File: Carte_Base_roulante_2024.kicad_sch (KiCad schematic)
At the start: 18 parts, among them J1 Screw_Terminal_01x02, J2 Screw_Terminal_01x02, J3 Screw_Terminal_01x02, U1 STM32G484RETx, U4 R-78E5.0-1.0

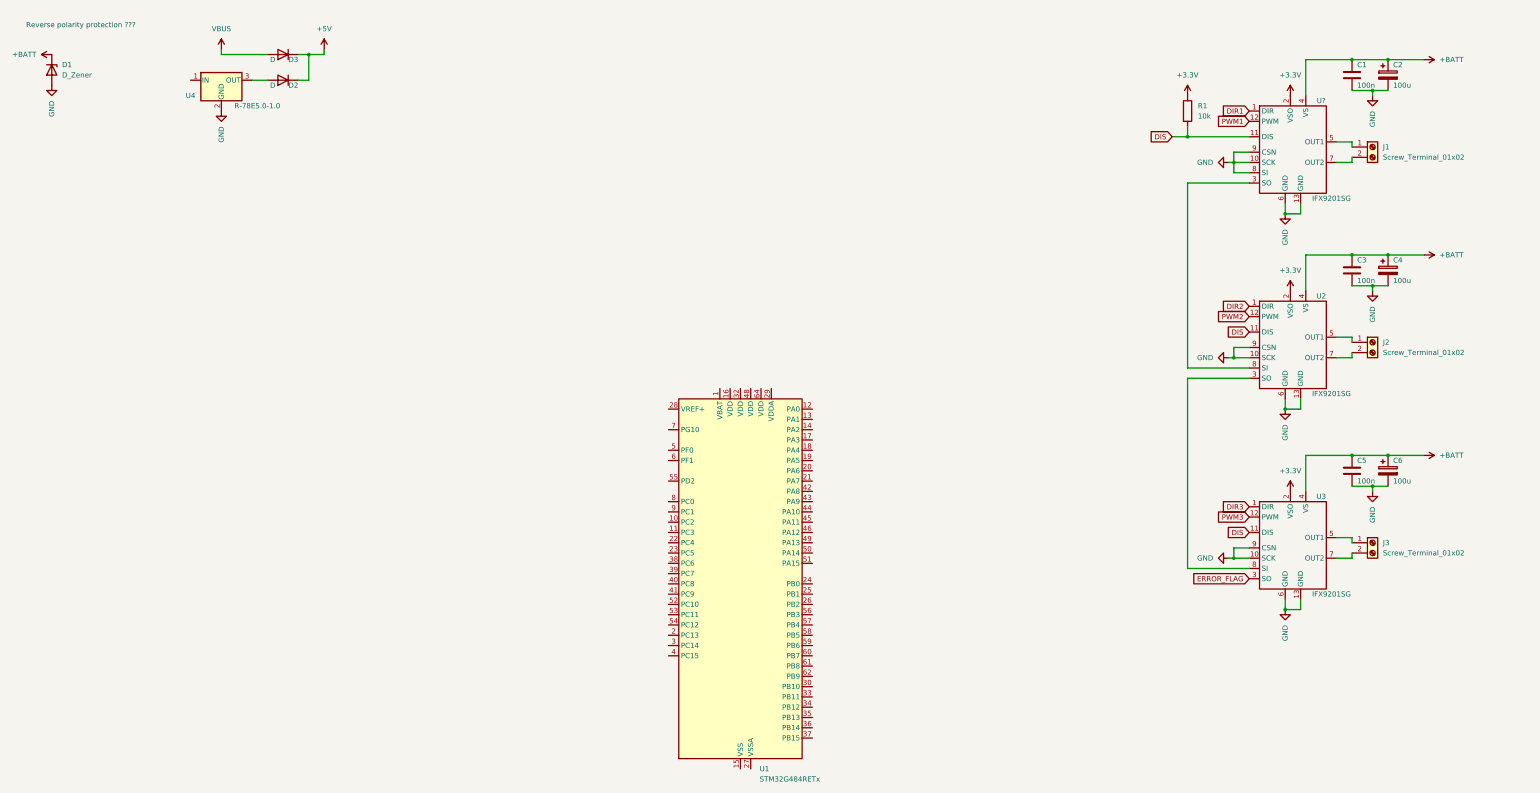
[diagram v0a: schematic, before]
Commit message: add capacitors
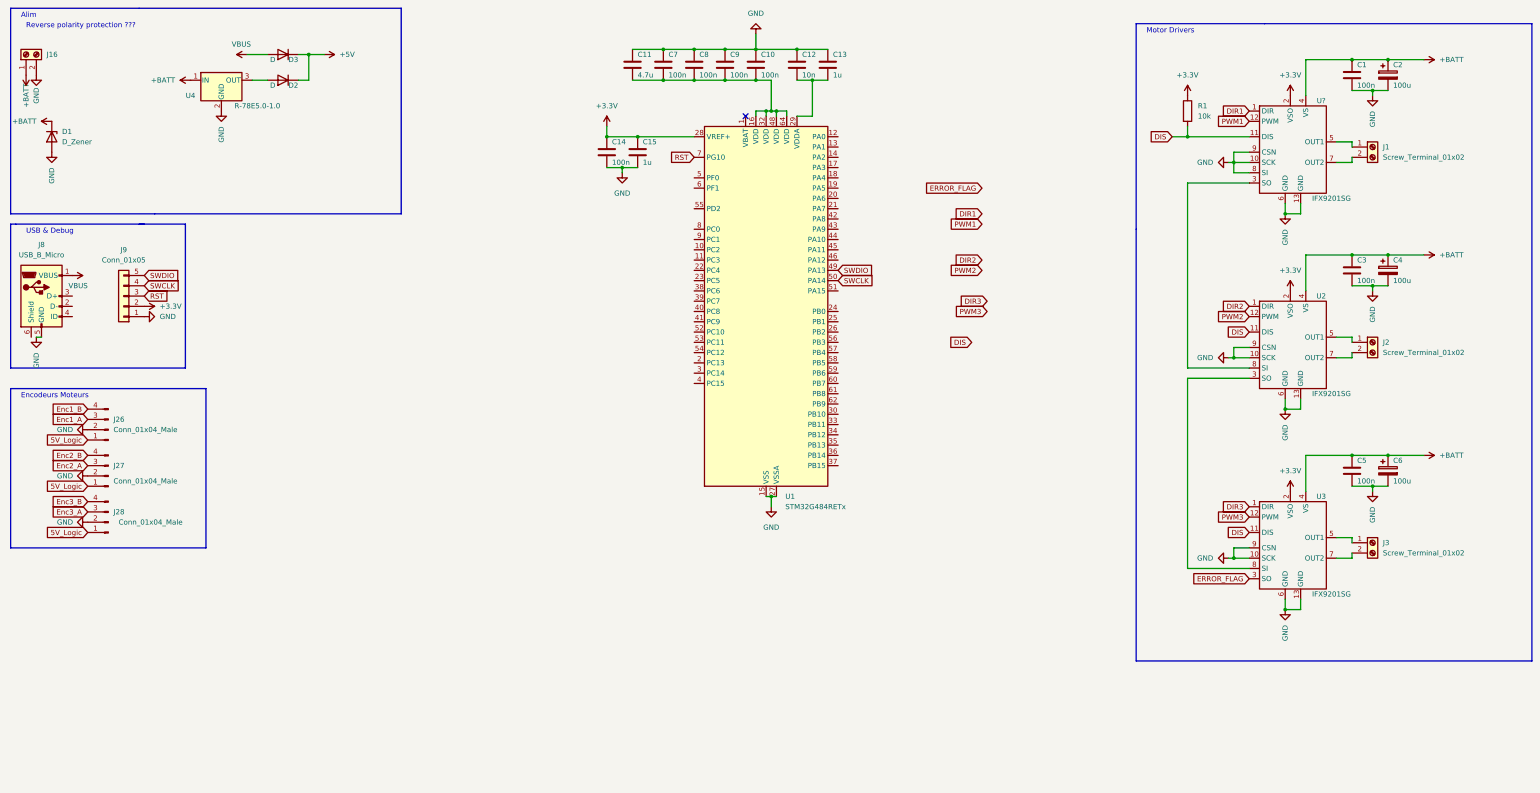
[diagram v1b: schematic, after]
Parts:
- added C10, C14, C7, C8, C9: 100n, Capacitor_SMD:C_0805_2012Metric, symbol Device:C
- added C11: 4.7u, symbol Device:C
- added C12: 10n, symbol Device:C
- added C13, C15: 1u, symbol Device:C
- added J16: Screw_Terminal_01x02, TerminalBlock:TerminalBlock_bornier-2_P5.08mm, symbol Connector:Screw_Terminal_01x02
- added J26, J27, J28: Conn_01x04_Male, library:HE14_EMBASE_1x04, symbol Connector:Conn_01x04_Male
- added J8: USB_B_Micro, symbol Connector:USB_B_Micro
- added J9: Conn_01x05, Connector_Molex:Molex_CLIK-Mate_502382-0570_1x05-1MP_P1.25mm_Vertical, symbol Connector_Generic:Conn_01x05
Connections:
- net +3.3V: now also U1.28 (VREF+), C14.1, C15.1, J9.2 (Pin_2)
- net +BATT: now also U4.1 (IN), J16.1 (Pin_1)
- net GND: now also U1.15 (VSS), U1.27 (VSSA), U1.31 (VSS), U1.47 (VSS), U1.63 (VSS), C10.1, C11.1, C12.1, C13.1, C14.2, C15.2, C7.1, C8.1, C9.1, J16.2 (Pin_2), J26.2 (Pin_2), J27.2 (Pin_2), J28.2 (Pin_2), J8.5 (GND), J9.1 (Pin_1)
- net VBUS: now also J8.1 (VBUS)
- net at U1.16 (VDD): now also U1.32 (VDD), U1.48 (VDD), U1.64 (VDD), C10.2, C11.2, C7.2, C8.2, C9.2
- net at U1.29 (VDDA): now also C12.2, C13.2
- net SWDIO: now reaches U1.49 (PA13)
- net SWDIO: now also J9.5 (Pin_5)
- net SWCLK: now reaches U1.50 (PA14)
- net SWCLK: now also J9.4 (Pin_4)
- net RST: now reaches U1.7 (PG10)
- net RST: now also J9.3 (Pin_3)
- new net 5V_Logic: J26.1 (Pin_1), J27.1 (Pin_1), J28.1 (Pin_1)
- new net Enc1_A: J26.3 (Pin_3)
- new net Enc1_B: J26.4 (Pin_4)
- new net Enc2_A: J27.3 (Pin_3)
- new net Enc2_B: J27.4 (Pin_4)
- new net Enc3_A: J28.3 (Pin_3)
- new net Enc3_B: J28.4 (Pin_4)
- no-connect marks 0 -> 1
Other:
- note added: "Alim"
- note added: "Encodeurs Moteurs"
- note added: "Motor Drivers"
- note added: "USB & Debug"
- moved on the sheet: D1, U1

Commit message: IMU + SPI
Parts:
- added U5: LSM6DSL, Package_LGA:LGA-14_3x2.5mm_P0.5mm_LayoutBorder3x4y, symbol Sensor_Motion:LSM6DSL
- U?: RS (none) -> https://fr.rs-online.com/web/p/drivers-de-moteur/1702333
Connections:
- net 5V_Logic is gone; now on net +5V: J26.1 (Pin_1), J27.1 (Pin_1), J28.1 (Pin_1)
- net DIR1: now also U1.41 (PC9)
- net DIR2: now also U1.44 (PA10)
- net DIR3: now also U1.46 (PA12)
- net DIS: now also U1.40 (PC8)
- net ERROR_FLAG: now also U1.39 (PC7)
- net Enc1_A: now also U1.12 (PA0)
- net Enc1_B: now also U1.13 (PA1)
- net Enc2_A: now also U1.20 (PA6)
- net Enc2_B: now also U1.21 (PA7)
- net Enc3_A: now also U1.60 (PB7)
- net Enc3_B: now also U1.59 (PB6)
- net PWM1: now also U1.42 (PA8)
- net PWM2: now also U1.43 (PA9)
- net PWM3: now also U1.45 (PA11)
- net UART4_TX: now reaches U1.52 (PC10)
- net UART4_RX: now reaches U1.53 (PC11)
- new net: U5.6 (GND), U5.7 (GND)
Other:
- note added: "Reverse polarity protection ??? Normalement on ne devrait pas brancher la batterie a l'enver donc non ?"
- note added: "Stm32"
- note removed: "Reverse polarity protection ???"
- moved on the sheet: C10, C11, C12, C13, C14, C15, C7, C8, C9, D2, D3, J16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

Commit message: usb + protection + cristal + leds + adc
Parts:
- removed J8: USB_B_Micro, symbol Connector:USB_B_Micro
- added C16, C17, C18: 100n, Capacitor_SMD:C_0805_2012Metric, symbol Device:C
- added D4: D_Zener, symbol Device:D_Zener
- added D5, D6, D7: LED, LED_SMD:LED_0603_1608Metric_Pad1.05x0.95mm_HandSolder, symbol Device:LED
- added J10: USB-C_12pin, ENAC_robotique:USB-C_HRO_C-31-M-12, symbol ENAC_robotique:USB-C_12pin
- added J8: Conn_01x03_Pin, Connector_PinHeader_2.54mm:PinHeader_1x03_P2.54mm_Vertical, symbol Connector:Conn_01x03_Pin
- added Q1: PMOS, symbol Simulation_SPICE:PMOS
- added R10, R5, R6: osef, Resistor_SMD:R_0805_2012Metric, symbol Device:R
- added R2, R3, R4: 10k, Resistor_SMD:R_0805_2012Metric, symbol Device:R
- added R7, R8: 5.1K, Resistor_SMD:R_0603_1608Metric_Pad0.98x0.95mm_HandSolder, symbol Device:R
- added R9: 40K, Resistor_SMD:R_0603_1608Metric_Pad0.98x0.95mm_HandSolder, symbol Device:R
- added SW1: SW_Push, symbol Switch:SW_Push
- added X1: ASCO, ENAC_robotique:Osc_ASCO, symbol ENAC_robotique:ASCO
- C11, C12, C13, C15: footprint (none) -> Capacitor_SMD:C_0805_2012Metric
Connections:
- net +3.3V: now also U5.5 (VDDIO), U5.8 (VDD), C16.2, C17.2, C18.1, SW1.1, X1.1 (TS), X1.4 (VDD)
- net +5V: now also R5.1
- net +BATT: now also D4.1 (K), Q1.3 (S); no longer J16.1 (Pin_1)
- net DIR1: now also U1.34 (PB12); no longer U1.41 (PC9)
- net DIR2: now also U1.33 (PB11); no longer U1.44 (PA10)
- net DIR3: now also U1.38 (PC6); no longer U1.46 (PA12)
- net DIS: now also U1.39 (PC7); no longer U1.40 (PC8)
- net ERROR_FLAG: now also U1.40 (PC8); no longer U1.39 (PC7)
- net GND: now also J16.1 (Pin_1), U5.2 (SDX), U5.3 (SCX), U5.6 (GND), U5.7 (GND), C16.1, C17.1, C18.2, D5.1 (K), D6.1 (K), D7.1 (K), J10.A1-B12 (GND), J10.B1-A12 (GND), J10.S (Shield), J8.1 (Pin_1), R2.2, R4.2, R7.2, R8.2, R9.2, X1.2 (GND); no longer J16.2 (Pin_2)
- net PWM1: now also U1.35 (PB13); no longer U1.42 (PA8)
- net PWM2: now also U1.36 (PB14); no longer U1.43 (PA9)
- net PWM3: now also U1.37 (PB15); no longer U1.45 (PA11)
- net UART4_RX: now also J8.2 (Pin_2)
- net UART4_TX: now also J8.3 (Pin_3)
- net VBUS: now also J10.A4-B9 (VBUS), J10.B4-A9 (VBUS)
- net OSCILATEUR: now reaches U1.5 (PF0)
- net OSCILATEUR: now also X1.3 (OUT)
- net IMU_INT1: now reaches U1.54 (PC12)
- net IMU_INT1: now also U5.4 (INT1)
- net SPI1_CS_IMU: now reaches U1.55 (PD2)
- net SPI1_CS_IMU: now also U5.12 (CS)
- net SPI1_SCK: now reaches U1.56 (PB3)
- net SPI1_SCK: now also U5.13 (SCL)
- net SPI1_MISO: now reaches U1.57 (PB4)
- net SPI1_MISO: now also U5.1 (SDO/SA0)
- net SPI1_MOSI: now reaches U1.58 (PB5)
- net SPI1_MOSI: now also U5.14 (SDA)
- net BOOT 0: now reaches U1.61 (PB8)
- net BOOT 0: now also R9.1, SW1.2
- new net: D5.2 (A), R5.2
- new net: D6.2 (A), R6.2
- new net: D4.2 (A), Q1.2 (G), R2.1
- new net: D7.2 (A), R10.2
- new net: J16.2 (Pin_2), Q1.1 (D), R3.1
- new net: J10.A5 (CC1), R7.1
- new net: J10.B5 (CC2), R8.1
- new net LED1: R10.1, U1.43 (PA9)
- new net LED2: R6.1, U1.44 (PA10)
- new net MEAS_VBAT: R3.2, R4.1, U1.42 (PA8)
- new net USB_DM: J10.A7 (D-1), J10.B7 (D-2), U1.45 (PA11)
- new net USB_DP: J10.A6 (D+1), J10.B6 (D+2), U1.46 (PA12)
- no-connect marks 1 -> 25
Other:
- note added: "Connectique USB UART DEBUG"
- note added: "Horloge"
- note added: "IMU"
- note added: "LEDS"
- note added: "valeurs des R_leds marqué "osef" car pn peux voir ça après ( il y en a 3 )"
- note removed: "Reverse polarity protection ??? Normalement on ne devrait pas brancher la batterie a l'enver donc non ?"
- note removed: "USB & Debug"
- moved on the sheet: C1, C10, C11, C12, C13, C14, C15, C2, C3, C4, C5, C6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

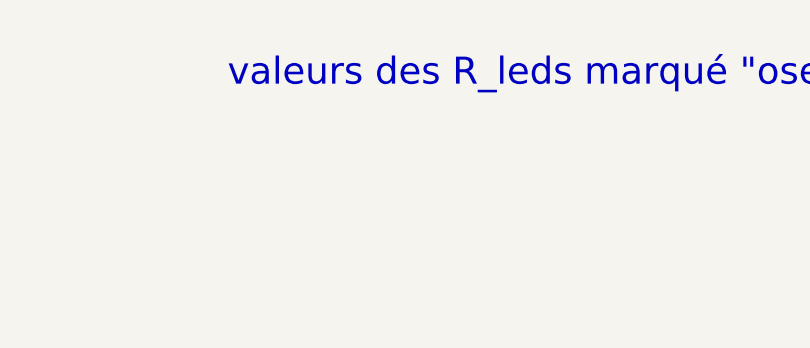
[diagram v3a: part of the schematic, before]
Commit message: add testpoints for SPI
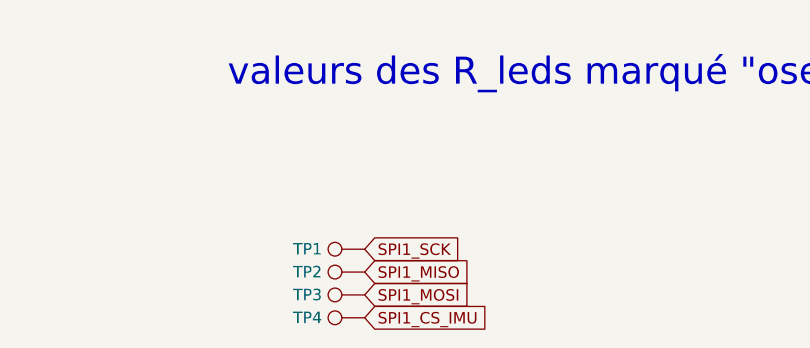
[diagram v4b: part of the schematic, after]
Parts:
- added TP1, TP2, TP3, TP4: TestPoint, TestPoint:TestPoint_Pad_D2.5mm, symbol Connector:TestPoint
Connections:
- net SPI1_CS_IMU: now also TP4.1
- net SPI1_MISO: now also TP2.1
- net SPI1_MOSI: now also TP3.1
- net SPI1_SCK: now also TP1.1
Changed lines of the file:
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@@
+    )
+  )
+  (global_label "SPI1_SCK" (shape input) (at 91.44 184.15 0) (fields_autoplaced)
+    (effects (font (size 1.27 1.27)) (justify left))
+    (property "Intersheetrefs" "${INTERSHEET_REFS}" (at 103.4361 184.15 0)
+      (effects (font (size 1.27 1.27)) (justify left) hide)
     )
   )
@@
     )
   )
+  (global_label "SPI1_MOSI" (shape input) (at 91.44 189.23 0) (fields_autoplaced)
+    (effects (font (size 1.27 1.27)) (justify left))
+    (property "Intersheetrefs" "${INTERSHEET_REFS}" (at 104.2828 189.23 0)
+      (effects (font (size 1.27 1.27)) (justify left) hide)
+    )
+  )
   (global_label "DIR2" (shape input) (at 311.15 90.17 180) (fields_autoplaced)
     (effects (font (size 1.27 1.27)) (justify right))
@@
     )
   )
+  (global_label "SPI1_CS_IMU" (shape input) (at 91.44 191.77 0) (fields_autoplaced)
+    (effects (font (size 1.27 1.27)) (justify left))
+    (property "Intersheetrefs" "${INTERSHEET_REFS}" (at 106.5204 191.77 0)
+      (effects (font (size 1.27 1.27)) (justify left) hide)
+    )
+  )
   (global_label "UART4_TX" (shape input) (at 105.41 111.76 0) (fields_autoplaced)
     (effects (font (size 1.27 1.27)) (justify left))
@@
     (effects (font (size 1.27 1.27)) (justify left))
     (property "Intersheetrefs" "${INTERSHEET_REFS}" (at 196.9928 107.95 0)
+      (effects (font (size 1.27 1.27)) (justify left) hide)
+    )
+  )
+  (global_label "SPI1_MISO" (shape input) (at 91.44 186.69 0) (fields_autoplaced)
+    (effects (font (size 1.27 1.27)) (justify left))
+    (property "Intersheetrefs" "${INTERSHEET_REFS}" (at 104.2828 186.69 0)
       (effects (font (size 1.27 1.27)) (justify left) hide)
     )
@@
     )
   )
+  (symbol (lib_id "Connector:TestPoint") (at 91.44 191.77 90) (unit 1)
+    (in_bom yes) (on_board yes) (dnp no)
+    (property "Reference" "TP4" (at 85.09 191.77 90)
+      (effects (font (size 1.27 1.27)))
+    )
+    (property "Value" "TestPoint" (at 77.47 191.77 90)
+      (effects (font (size 1.27 1.27)) hide)
+    )
+    (property "Footprint" "TestPoint:TestPoint_Pad_D2.5mm" (at 91.44 186.69 0)
+      (effects (font (size 1.27 1.27)) hide)
+    )
+    (property "Datasheet" "~" (at 91.44 186.69 0)
+      (effects (font (size 1.27 1.27)) hide)
+    )
+    (pin "1")
+    (instances
+      (project "Carte_Base_roulante_2024"
+        (path "/f941aee9-3a44-439b-9c30-032c53e86031"
+          (reference "TP4") (unit 1)
+        )
+      )
+    )
+  )
   (symbol (lib_id "Device:C") (at 140.97 36.83 0) (unit 1)
     (in_bom yes) (on_board yes) (dnp no)
@@
         (path "/f941aee9-3a44-439b-9c30-032c53e86031"
           (reference "C11") (unit 1)
+        )
+      )
+    )
+  )
+  (symbol (lib_id "Connector:TestPoint") (at 91.44 186.69 90) (unit 1)
+    (in_bom yes) (on_board yes) (dnp no)
+    (property "Reference" "TP2" (at 85.09 186.69 90)
+      (effects (font (size 1.27 1.27)))
+    )
+    (property "Value" "TestPoint" (at 77.47 186.69 90)
+      (effects (font (size 1.27 1.27)) hide)
+    )
+    (property "Footprint" "TestPoint:TestPoint_Pad_D2.5mm" (at 91.44 181.61 0)
+      (effects (font (size 1.27 1.27)) hide)
+    )
+    (property "Datasheet" "~" (at 91.44 181.61 0)
+      (effects (font (size 1.27 1.27)) hide)
+    )
+    (pin "1")
+    (instances
+      (project "Carte_Base_roulante_2024"
+        (path "/f941aee9-3a44-439b-9c30-032c53e86031"
+          (reference "TP2") (unit 1)
         )
       )
@@
     )
   )
+  (symbol (lib_id "Connector:TestPoint") (at 91.44 189.23 90) (unit 1)
+    (in_bom yes) (on_board yes) (dnp no)
+    (property "Reference" "TP3" (at 85.09 189.23 90)
+      (effects (font (size 1.27 1.27)))
+    )
+    (property "Value" "TestPoint" (at 77.47 189.23 90)
+      (effects (font (size 1.27 1.27)) hide)
+    )
+    (property "Footprint" "TestPoint:TestPoint_Pad_D2.5mm" (at 91.44 184.15 0)
+      (effects (font (size 1.27 1.27)) hide)
+    )
+    (property "Datasheet" "~" (at 91.44 184.15 0)
+      (effects (font (size 1.27 1.27)) hide)
+    )
+    (pin "1")
+    (instances
+      (project "Carte_Base_roulante_2024"
+        (path "/f941aee9-3a44-439b-9c30-032c53e86031"
+          (reference "TP3") (unit 1)
+        )
+      )
+    )
+  )
   (symbol (lib_id "ENAC_robotique:IFX9201SG") (at 321.31 149.86 0) (unit 1)
     (in_bom yes) (on_board yes) (dnp no)
@@
         )
       )
+    )
+  )
+  (symbol (lib_id "Connector:TestPoint") (at 91.44 184.15 90) (unit 1)
+    (in_bom yes) (on_board yes) (dnp no)
+    (property "Reference" "TP1" (at 85.09 184.15 90)
+      (effects (font (size 1.27 1.27)))
+    )
+    (property "Value" "TestPoint" (at 77.47 184.15 90)
+      (effects (font (size 1.27 1.27)) hide)
+    )
+    (property "Footprint" "TestPoint:TestPoint_Pad_D2.5mm" (at 91.44 179.07 0)
+      (effects (font (size 1.27 1.27)) hide)
+    )
+    (property "Datasheet" "~" (at 91.44 179.07 0)
+      (effects (font (size 1.27 1.27)) hide)
+    )
+    (pin "1")
+    (instances
+      (project "Carte_Base_roulante_2024"
+        (path "/f941aee9-3a44-439b-9c30-032c53e86031"
+          (reference "TP1") (unit 1)
+        )
+      )

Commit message: ajout empreintes wip
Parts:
- removed D1: D_Zener, symbol Device:D_Zener
- removed J26, J27, J28: Conn_01x04_Male, library:HE14_EMBASE_1x04, symbol Connector:Conn_01x04_Male
- added C19: 470n, Capacitor_SMD:C_0805_2012Metric, symbol Device:C
- added C20, C21, C22: 10u, Capacitor_SMD:C_0805_2012Metric, symbol Device:C
- added C23, C24: 10u, Capacitor_SMD:C_1206_3216Metric, symbol Device:C
- added IC1: LM3940IMP-3.3, ENAC_robotique:LM3940IMP, symbol ENAC_robotique:LM3940IMP-3.3
- added J11: ENC1, Connector_PinHeader_2.54mm:PinHeader_1x04_P2.54mm_Vertical, symbol Connector:Conn_01x04_Pin
- added J4: ENC2, Connector_PinHeader_2.54mm:PinHeader_1x04_P2.54mm_Vertical, symbol Connector:Conn_01x04_Pin
- added J5: ENC3, Connector_PinHeader_2.54mm:PinHeader_1x04_P2.54mm_Vertical, symbol Connector:Conn_01x04_Pin
- D2, D3: footprint (none) -> Diode_SMD:Nexperia_CFP3_SOD-123W
- D4: footprint (none) -> Diode_SMD:D_SOD-523
- D5: footprint LED_SMD:LED_0603_1608Metric_Pad1.05x0.95mm_HandSolder -> LED_SMD:LED_0603_1608Metric
- D6: value LED -> LED2
- D7: value LED -> LED1
- R3: value 10k -> 53k
- R7, R8: footprint Resistor_SMD:R_0603_1608Metric_Pad0.98x0.95mm_HandSolder -> Resistor_SMD:R_0603_1608Metric
- R9: footprint Resistor_SMD:R_0603_1608Metric_Pad0.98x0.95mm_HandSolder -> Resistor_SMD:R_0805_2012Metric
- SW1: footprint (none) -> ENAC_robotique:SWITCH_DTSM31NV; RS (none) -> https://fr.rs-online.com/web/p/interrupteurs-tactiles/37863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; Ref RS (none) -> 378-6325
- gave numbers to parts that had none: 1
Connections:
- net +3.3V: now also C10.2, C11.2, C12.2, C13.2, C7.2, C8.2, C9.2, U1.16 (VDD), U1.29 (VDDA), U1.32 (VDD), U1.48 (VDD), U1.64 (VDD), C20.1, C21.1, C22.1, IC1.3 (OUT)
- net +5V: now also C19.1, IC1.1 (IN), J11.1 (Pin_1), J4.1 (Pin_1), J5.1 (Pin_1)
- net +BATT: now also C23.1
- net Enc1_A: now also J11.3 (Pin_3)
- net Enc1_B: now also J11.4 (Pin_4)
- net Enc2_A: now also J4.3 (Pin_3)
- net Enc2_B: now also J4.4 (Pin_4)
- net Enc3_A: now also J5.3 (Pin_3)
- net Enc3_B: now also J5.4 (Pin_4)
- net GND: now also C19.2, C20.2, C21.2, C22.2, C23.2, C24.2, IC1.2 (GND), IC1.4 (TAB), J11.2 (Pin_2), J4.2 (Pin_2), J5.2 (Pin_2)
- net UART4_RX: now also J8.3 (Pin_3); no longer J8.2 (Pin_2)
- net UART4_TX: now also J8.2 (Pin_2); no longer J8.3 (Pin_3)
- net at D2.2 (A), U4.3 (OUT): now also C24.1
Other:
- note added: "Pads Pour Analyseur logique"
- note added: "valeurs des R_leds marqué "osef" car on peux voir ça après ( il y en a 3 )"
- note removed: "valeurs des R_leds marqué "osef" car pn peux voir ça après ( il y en a 3 )"
- moved on the sheet: C18, D2, D3, D4, D5, D6, D7, J10, J16, J8, J9, Q1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

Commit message: placement préliminaire
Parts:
- removed Q1: PMOS, symbol Simulation_SPICE:PMOS
- added Q2: IRF7424, Package_SO:SOIC-8_3.9x4.9mm_P1.27mm, symbol Transistor_FET:IRF7404
- D5: value LED -> LED_ALIM
- DEBUG1: renamed from J9; value Conn_01x05 -> DEBUG
- J16: value Screw_Terminal_01x02 -> ALIM
- MOT1: renamed from J1; value Screw_Terminal_01x02 -> MOT1
- MOT2: renamed from J2; value Screw_Terminal_01x02 -> MOT2
- MOT3: renamed from J3; value Screw_Terminal_01x02 -> MOT3
- renumbered U5 to IMU1, D7 to LED1, D6 to LED2, X1 to QUARTZ1, SW1 to SWITCH1, TP4 to TP_CS1, TP2 to TP_MISO1, TP3 to TP_MOSI1, TP1 to TP_SCK1, U4 to Transfo18->5, IC1 to Transfo5->3.3, J8 to UART4, J10 to USB-C1, D4 to ZENER1
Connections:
- net +BATT: now also Q2.1 (S), Q2.2 (S), Q2.3 (S)
- net at R2.1, ZENER1.2 (A): now also Q2.4 (G)
- net at J16.2 (Pin_2), R3.1: now also Q2.5 (D), Q2.6 (D), Q2.7 (D), Q2.8 (D)
